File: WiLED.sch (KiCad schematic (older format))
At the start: 57 parts, among them J1 Mount, J2 Mount, J3 Mount, J4 Mount, P1 Serial to USB, P2 DC In, P4 LED Out, SW1 Reset, SW2 Boot, SW3 Toggle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

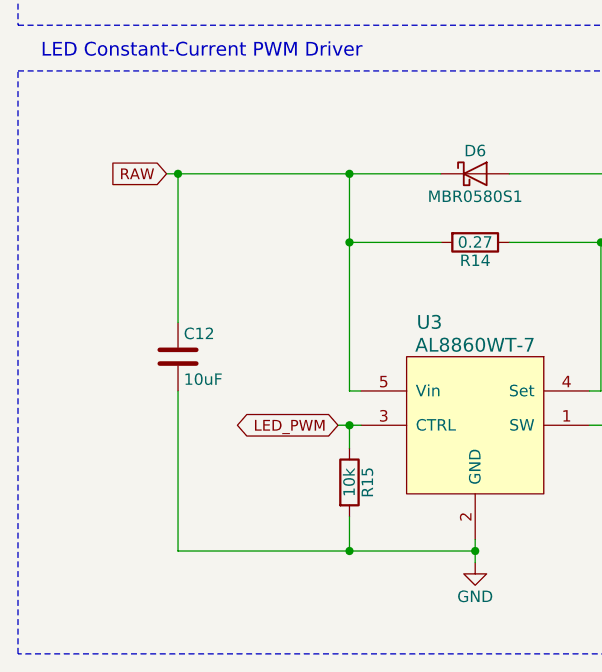
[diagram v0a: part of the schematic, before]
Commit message: Re-do layout, for v3.0
Having started the 3D CAD for the enclosure, it seems that the PCB is
able to be slightly wider than previously planned. To make the most of
this new width, a complete rearrange has been done - the PCB is now a
square shape.
Routing has been completed on this new layout, vias still need to be
added.
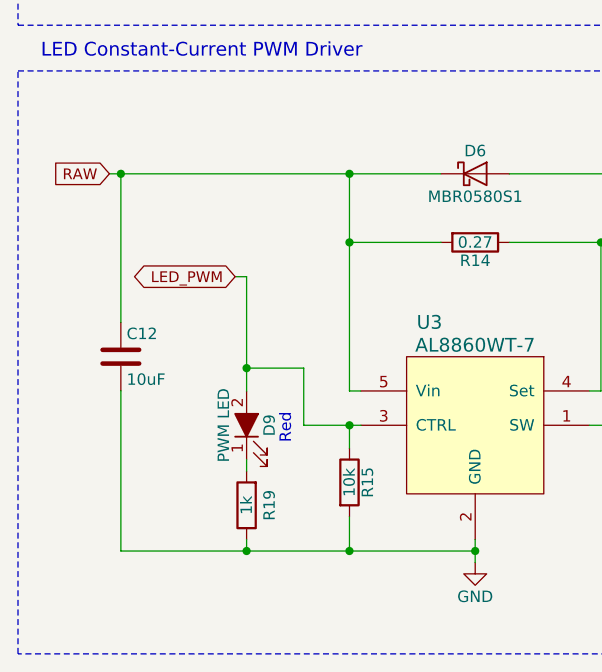
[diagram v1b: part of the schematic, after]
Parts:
- added D9: PWM LED, custom-footprints:WL-SMCW, symbol WiLED-rescue:LED_ALT
- added R19: 1k, Resistor_SMD:R_0603_1608Metric, symbol WiLED-rescue:R
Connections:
- net GND: now also R19.1
- net LED_PWM: now also D9.2 (A)
- new net: D9.1 (K), R19.2
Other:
- moved on the sheet: C12
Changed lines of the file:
@@
 Sheet 1 1
 Title "WiLED ESP32 Base"
-Date "2018-09-02"
+Date "2018-09-15"
 Rev "2.1"
 Comp "Sean Lanigan"
@@
 Wire Notes Line
 	650  5100 4950 5100
-Text GLabel 2050 6650 0    47   BiDi ~ 0
+Text GLabel 1600 6000 0    47   BiDi ~ 0
 LED_PWM
-Wire Wire Line
-	2050 6650 2100 6650
 Connection ~ 2100 6650
 $Comp
@@
 	2650 7150 2650 7200
 Wire Wire Line
-	1350 7200 2100 7200
+	1100 7200 1650 7200
 Connection ~ 2650 7200
-Text GLabel 1300 5550 0    47   Input ~ 0
+Text GLabel 1050 5550 0    47   Input ~ 0
 RAW
 $Comp
@@
 $EndComp
 Wire Wire Line
-	1300 5550 1350 5550
+	1050 5550 1100 5550
 Wire Wire Line
 	2100 5550 2100 5850
@@
 	2100 5850 2500 5850
 Connection ~ 2100 5850
-Connection ~ 2100 5550
 Wire Wire Line
 	3200 5850 3200 6500
@@
 L WiLED-rescue:C C12
 U 1 1 5B269A23
-P 1350 6350
-F 0 "C12" H 1375 6450 50  0000 L CNN
-F 1 "10uF" H 1375 6250 50  0000 L CNN
-F 2 "Capacitor_SMD:C_1206_3216Metric" H 1388 6200 50  0001 C CNN
-F 3 "" H 1350 6350 50  0000 C CNN
-	1    1350 6350
-	1    0    0    -1
-$EndComp
-Connection ~ 1350 5550
-Connection ~ 2100 7200
-Wire Wire Line
-	1350 6200 1350 5550
-Wire Wire Line
-	1350 6500 1350 7200
+P 1100 6350
+F 0 "C12" H 1125 6450 50  0000 L CNN
+F 1 "10uF" H 1125 6250 50  0000 L CNN
+F 2 "Capacitor_SMD:C_1206_3216Metric" H 1138 6200 50  0001 C CNN
+F 3 "" H 1100 6350 50  0000 C CNN
+	1    1100 6350
+	1    0    0    -1
+$EndComp
+Connection ~ 1100 5550
+Wire Wire Line
+	1100 6200 1100 5550
+Wire Wire Line
+	1100 6500 1100 7200
 Wire Wire Line
 	2100 6750 2100 6650
@@
 	2100 5550 2500 5550
 Wire Wire Line
-	1350 5550 2100 5550
-Wire Wire Line
 	2100 7200 2650 7200
 Wire Wire Line
@@
 	1    0    0    -1
 $EndComp
+$Comp
+L WiLED-rescue:LED_ALT D9
+U 1 1 5B9DC567
+P 1650 6650
+F 0 "D9" H 1650 6550 50  0000 C CNN
+F 1 "PWM LED" H 1650 6750 50  0000 C CNN
+F 2 "custom-footprints:WL-SMCW" H 1650 6650 50  0001 C CNN
+F 3 "" H 1650 6650 50  0000 C CNN
+	1    1650 6650
+	0    -1   -1   0
+$EndComp
+$Comp
+L WiLED-rescue:R R19
+U 1 1 5B9DC573
+P 1650 7000
+F 0 "R19" V 1550 7000 50  0000 C CNN
+F 1 "1k" V 1650 7000 50  0000 C CNN
+F 2 "Resistor_SMD:R_0603_1608Metric" V 1580 7000 50  0001 C CNN
+F 3 "" H 1650 7000 50  0000 C CNN
+	1    1650 7000
+	-1   0    0    1
+$EndComp
+Text Notes 1850 6600 3    50   ~ 0
+Red
+Wire Wire Line
+	1650 6800 1650 6850
+Wire Wire Line
+	1650 7150 1650 7200
+Connection ~ 1650 7200
+Wire Wire Line
+	1900 6650 1900 6400
+Wire Wire Line
+	1900 6400 1650 6400
+Wire Wire Line
+	1650 6400 1650 6500
+Wire Wire Line
+	1900 6650 2100 6650
+Wire Wire Line
+	1600 6000 1650 6000
+Wire Wire Line
+	1650 6000 1650 6400
+Connection ~ 1650 6400
+Wire Wire Line
+	1100 5550 2100 5550
+Connection ~ 2100 5550
+Wire Wire Line
+	1650 7200 2100 7200
+Connection ~ 2100 7200
 $EndSCHEMATC

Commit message: Change R14 to 0603 size
R14 was originally an 0603 in v1.0, but was changed to an 0805 - looking
at parts, 0603 are cheaper and still have the required values and
tolerances, so 0603 should be used instead.
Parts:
- R14: footprint Resistor_SMD:R_0805_2012Metric -> Resistor_SMD:R_0603_1608Metric_Pad1.05x0.95mm_HandSolder
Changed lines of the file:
@@
 Sheet 1 1
 Title "WiLED ESP32 Base"
-Date "2018-09-24"
+Date "2018-10-02"
 Rev "3.0"
 Comp "Sean Lanigan"
@@
 F 0 "R14" V 2730 5850 50  0000 C CNN
 F 1 "0.27" V 2650 5850 50  0000 C CNN
-F 2 "Resistor_SMD:R_0805_2012Metric" V 2580 5850 50  0001 C CNN
+F 2 "Resistor_SMD:R_0603_1608Metric_Pad1.05x0.95mm_HandSolder" V 2580 5850 50  0001 C CNN
 F 3 "" H 2650 5850 50  0000 C CNN
 	1    2650 5850

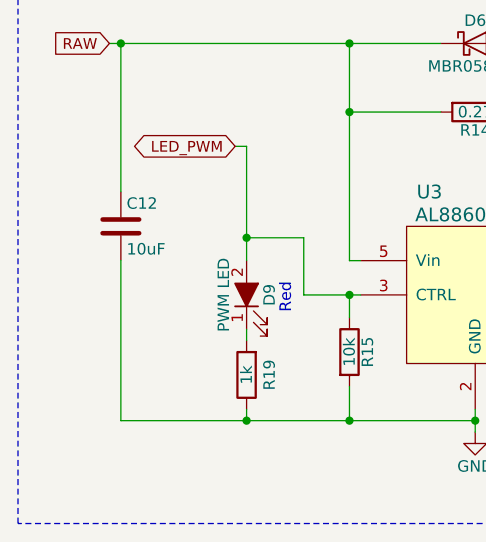
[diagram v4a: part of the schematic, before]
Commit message: Change C12 and C13 to through-hole electrolytic caps
C12 and C13 were initially MLCCs, but these are harder to obtain and are
more expensive than electrolytics - for this use case, the swap should
be acceptable.
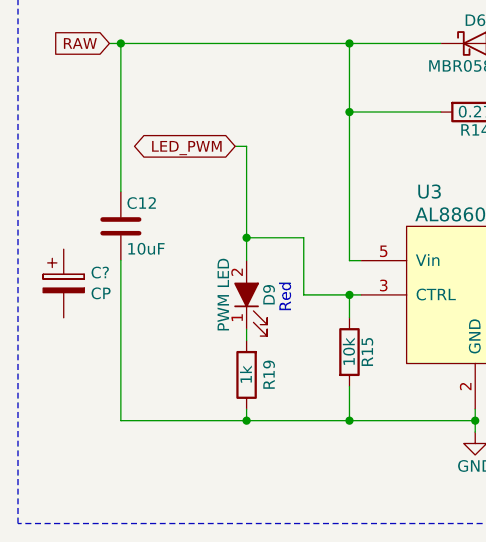
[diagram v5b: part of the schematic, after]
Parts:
- added C?: CP, symbol Device:CP
- C12, C13: footprint Capacitor_SMD:C_1206_3216Metric -> Capacitor_THT:CP_Radial_D5.0mm_P2.00mm
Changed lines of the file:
@@
 Sheet 1 1
 Title "WiLED ESP32 Base"
-Date "2018-10-02"
+Date "2018-10-08"
 Rev "3.0"
 Comp "Sean Lanigan"
@@
 F 0 "C12" H 1125 6450 50  0000 L CNN
 F 1 "10uF" H 1125 6250 50  0000 L CNN
-F 2 "Capacitor_SMD:C_1206_3216Metric" H 1138 6200 50  0001 C CNN
+F 2 "Capacitor_THT:CP_Radial_D5.0mm_P2.00mm" H 1138 6200 50  0001 C CNN
 F 3 "" H 1100 6350 50  0000 C CNN
 	1    1100 6350
@@
 F 0 "C13" H 8900 4500 50  0000 L CNN
 F 1 "10uF" H 8900 4300 50  0000 L CNN
-F 2 "Capacitor_SMD:C_1206_3216Metric" H 8888 4250 50  0001 C CNN
+F 2 "Capacitor_THT:CP_Radial_D5.0mm_P2.00mm" H 8888 4250 50  0001 C CNN
 F 3 "~" H 8850 4400 50  0001 C CNN
 	1    8850 4400
@@
 	1650 7200 2100 7200
 Connection ~ 2100 7200
+$Comp
+L Device:CP C?
+U 1 1 5BB80A82
+P 850 6600
+F 0 "C?" H 968 6646 50  0000 L CNN
+F 1 "CP" H 968 6555 50  0000 L CNN
+F 2 "" H 888 6450 50  0001 C CNN
+F 3 "~" H 850 6600 50  0001 C CNN
+	1    850  6600
+	1    0    0    -1
+$EndComp
 $EndSCHEMATC

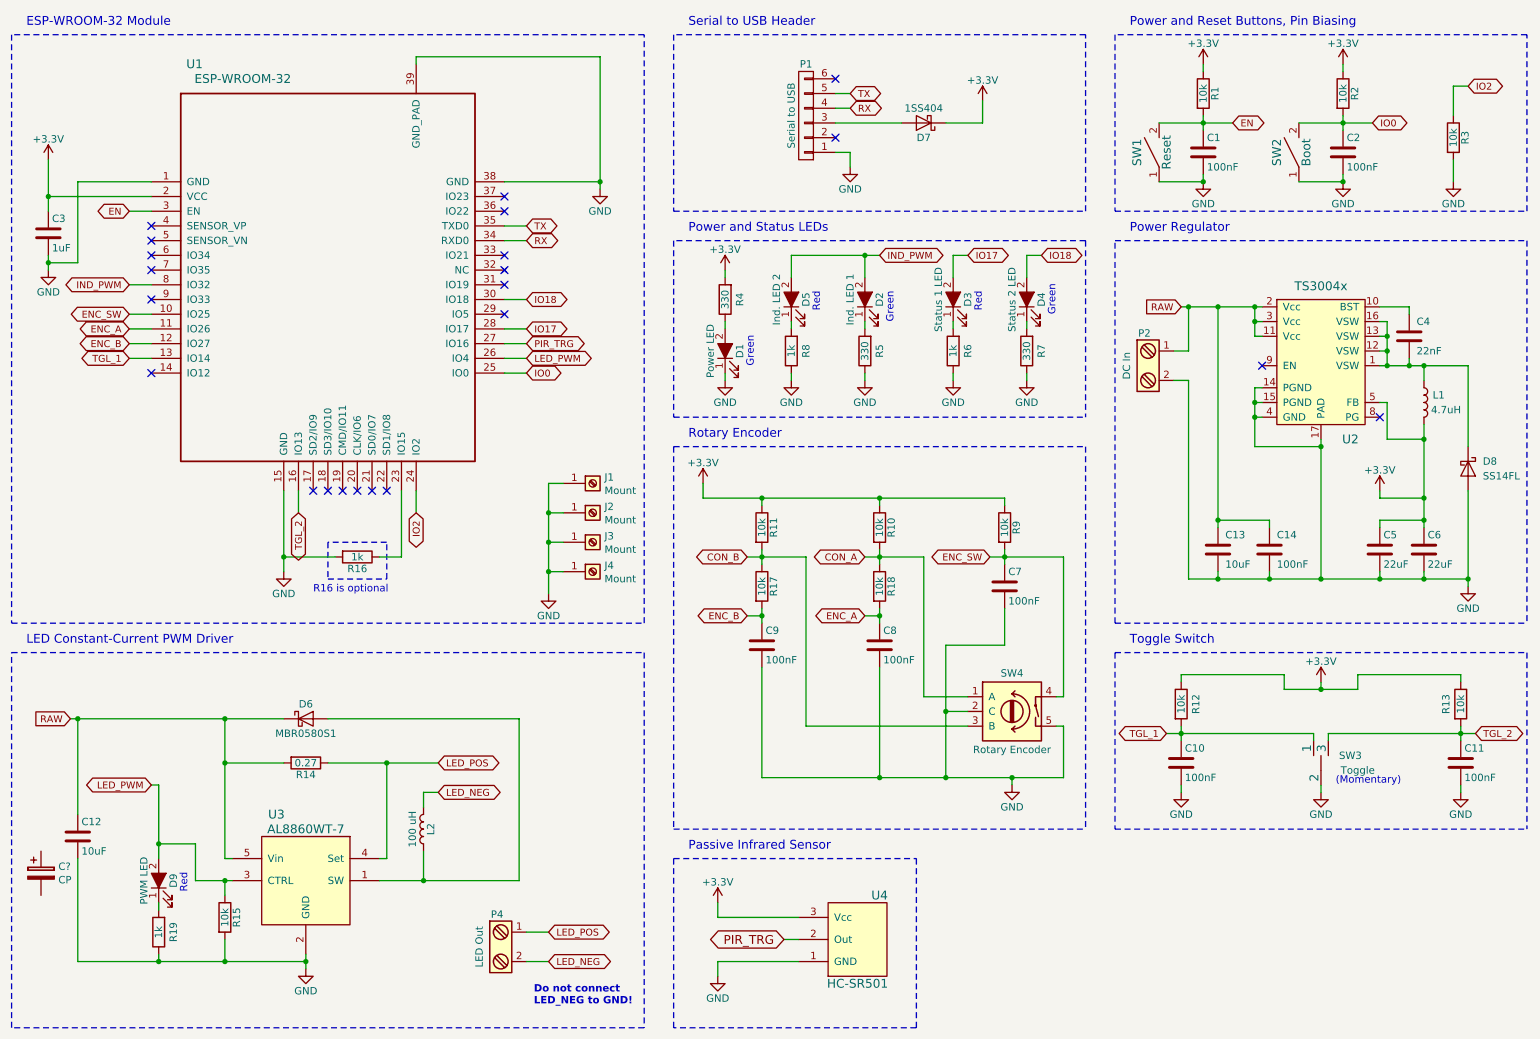
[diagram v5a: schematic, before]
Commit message: Update model for pin headers, revise ground vias
Updated the footprint for the 6-pin header P1, to one with a 3D model.
Revised some ground plane vias, and re-routed some tracks to give
slightly more contiguous ground plane regions.
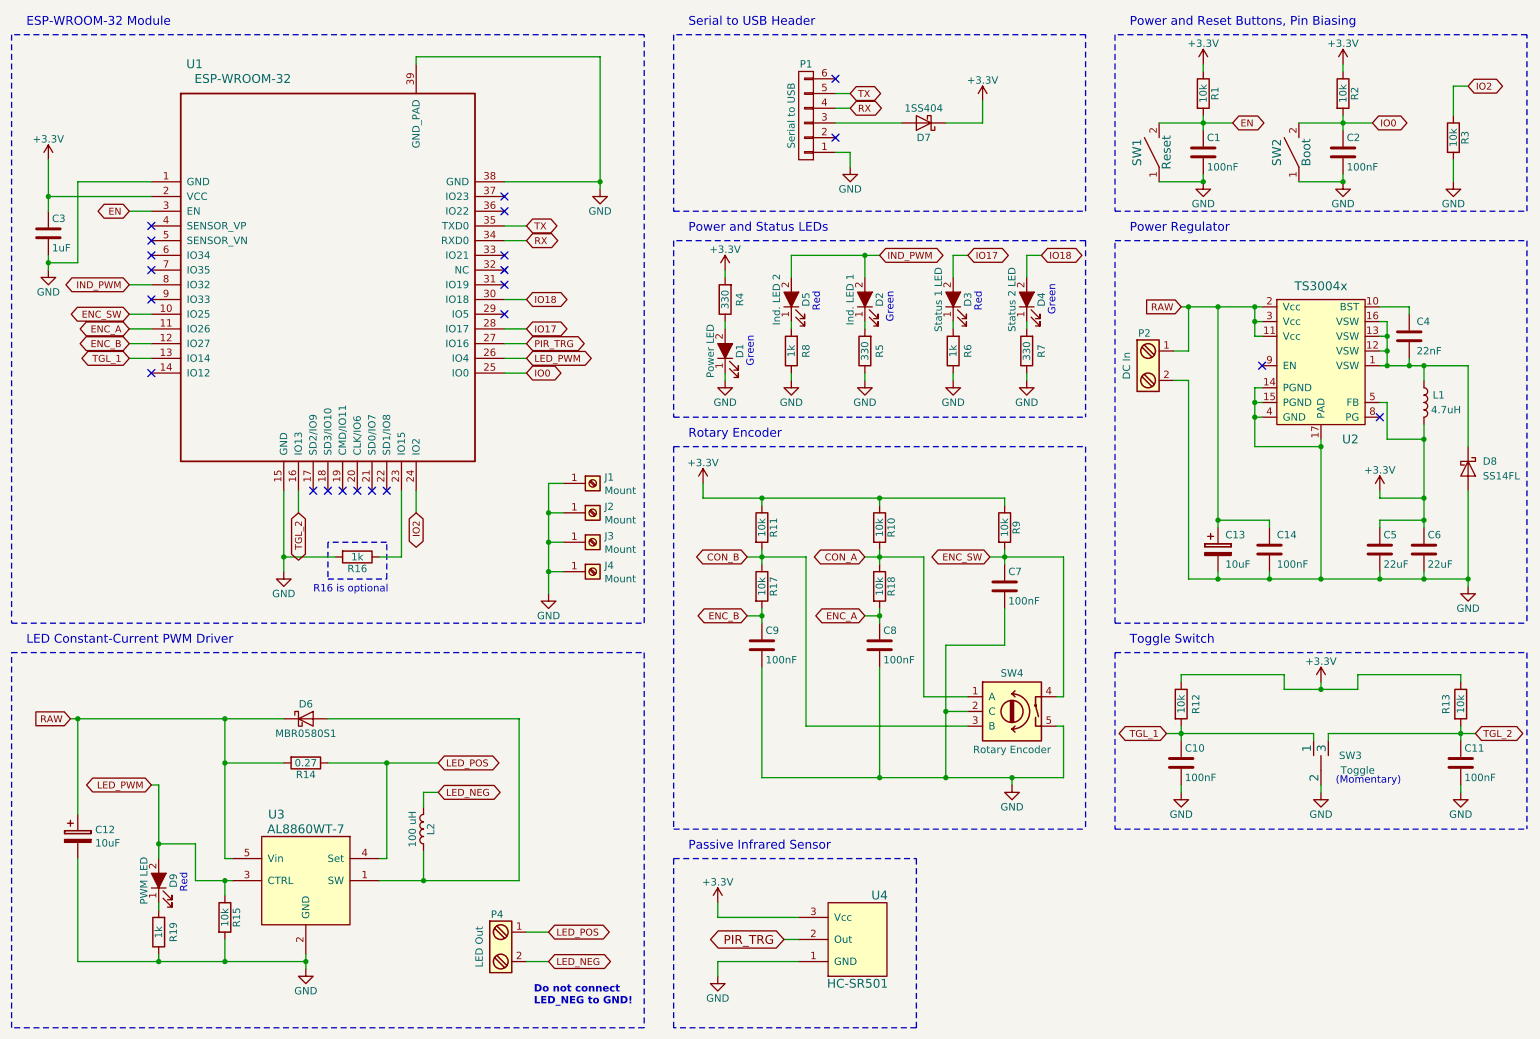
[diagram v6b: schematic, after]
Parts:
- removed C12: 10uF, Capacitor_THT:CP_Radial_D5.0mm_P2.00mm, symbol WiLED-rescue:C
- removed C13: 10uF, Capacitor_THT:CP_Radial_D5.0mm_P2.00mm, symbol Device:C
- added C13: 10uF, symbol Device:CP
- C12: renamed from C?; value CP -> 10uF
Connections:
- net GND: now also C12.2, C13.2
- net RAW: now also C12.1, C13.1
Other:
- moved on the sheet: C12
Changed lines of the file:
@@
 Sheet 1 1
 Title "WiLED ESP32 Base"
-Date "2018-10-08"
+Date "2018-10-10"
 Rev "3.0"
 Comp "Sean Lanigan"
@@
 Wire Wire Line
 	3200 6500 3150 6500
-$Comp
-L WiLED-rescue:C C12
-U 1 1 5B269A23
-P 1100 6350
-F 0 "C12" H 1125 6450 50  0000 L CNN
-F 1 "10uF" H 1125 6250 50  0000 L CNN
-F 2 "Capacitor_THT:CP_Radial_D5.0mm_P2.00mm" H 1138 6200 50  0001 C CNN
-F 3 "" H 1100 6350 50  0000 C CNN
-	1    1100 6350
-	1    0    0    -1
-$EndComp
 Connection ~ 1100 5550
 Wire Wire Line
@@
 	8650 2750 8600 2750
 Connection ~ 8650 2750
-$Comp
-L Device:C C13
-U 1 1 5B8B5F13
-P 8850 4400
-F 0 "C13" H 8900 4500 50  0000 L CNN
-F 1 "10uF" H 8900 4300 50  0000 L CNN
-F 2 "Capacitor_THT:CP_Radial_D5.0mm_P2.00mm" H 8888 4250 50  0001 C CNN
-F 3 "~" H 8850 4400 50  0001 C CNN
-	1    8850 4400
-	1    0    0    -1
-$EndComp
 Wire Wire Line
 	10250 4600 10250 4550
@@
 Connection ~ 2100 7200
 $Comp
-L Device:CP C?
+L Device:CP C12
 U 1 1 5BB80A82
-P 850 6600
-F 0 "C?" H 968 6646 50  0000 L CNN
-F 1 "CP" H 968 6555 50  0000 L CNN
-F 2 "" H 888 6450 50  0001 C CNN
-F 3 "~" H 850 6600 50  0001 C CNN
-	1    850  6600
-	1    0    0    -1
-$EndComp
+P 1100 6350
+F 0 "C12" H 1218 6396 50  0000 L CNN
+F 1 "10uF" H 1218 6305 50  0000 L CNN
+F 2 "" H 1138 6200 50  0001 C CNN
+F 3 "~" H 1100 6350 50  0001 C CNN
+	1    1100 6350
+	1    0    0    -1
+$EndComp
+$Comp
+L Device:CP C13
+U 1 1 5BBEE2BD
+P 8850 4400
+F 0 "C13" H 8900 4500 50  0000 L CNN
+F 1 "10uF" H 8900 4300 50  0000 L CNN
+F 2 "" H 8888 4250 50  0001 C CNN
+F 3 "~" H 8850 4400 50  0001 C CNN
+	1    8850 4400
+	1    0    0    -1
+$EndComp

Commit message: Change terminal blocks to 3.5 mm type
The previous terminal blocks were the 5.08 mm type, which are quite
large - larger than is needed. The 3.5 mm type should be enough, so
changed the footprints and re-routed where needed.
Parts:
- P2, P4: footprint custom-footprints:Terminal -> TerminalBlock_MetzConnect:TerminalBlock_MetzConnect_Type059_RT06302HBWC_1x02_P3.50mm_Horizontal
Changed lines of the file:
@@
 F 0 "P2" H 8350 3400 50  0000 C TNN
 F 1 "DC In" V 8200 3150 50  0000 C TNN
-F 2 "custom-footprints:Terminal" H 8350 2925 50  0001 C CNN
+F 2 "TerminalBlock_MetzConnect:TerminalBlock_MetzConnect_Type059_RT06302HBWC_1x02_P3.50mm_Horizontal" H 8350 2925 50  0001 C CNN
 F 3 "" H 8325 3150 50  0001 C CNN
 	1    8350 3150
@@
 F 0 "P4" H 3950 7350 50  0000 C TNN
 F 1 "LED Out" V 3800 7100 50  0000 C TNN
-F 2 "custom-footprints:Terminal" H 3950 6875 50  0001 C CNN
+F 2 "TerminalBlock_MetzConnect:TerminalBlock_MetzConnect_Type059_RT06302HBWC_1x02_P3.50mm_Horizontal" H 3950 6875 50  0001 C CNN
 F 3 "" H 3925 7100 50  0001 C CNN
 	1    3950 7100
